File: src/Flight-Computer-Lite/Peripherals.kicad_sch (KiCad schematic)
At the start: 36 parts, among them P3 USB, P4 1984659, Q1 QS5U17TR, Q2 QS5U17TR, U3 SST25VF040B-50-4I-S2AE-T, U4 CP2102-GMR(QFN28), U5 TS391IYLT, U6 BMP390, U7 TS391IYLT, U8 TS391IYLT

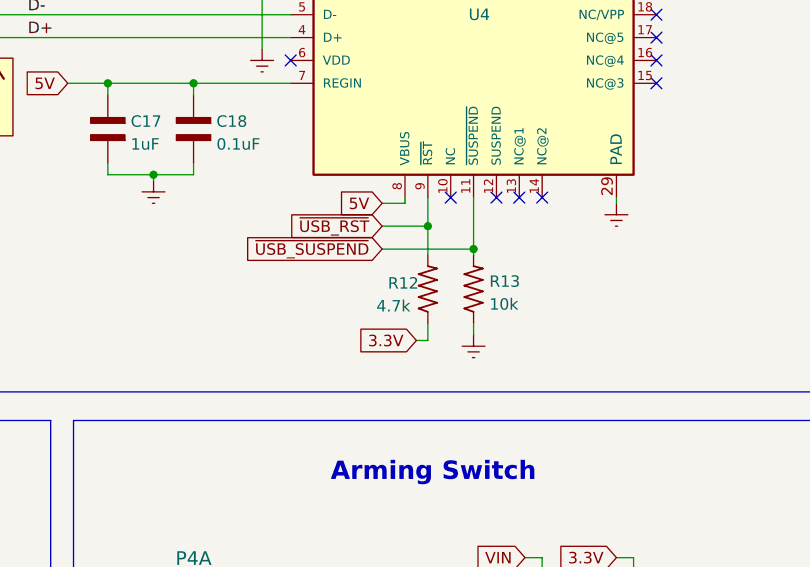
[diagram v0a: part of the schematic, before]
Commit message: imported footprints into layout
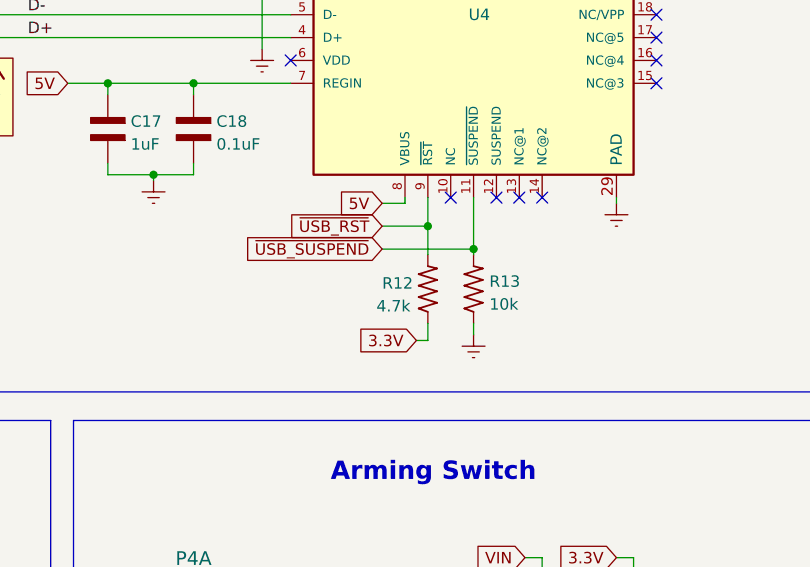
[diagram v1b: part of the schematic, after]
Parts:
- B2: footprint SW_PTS647SM38SMTR2LFS_CNK -> Flight-Computer-Lite:PTS647SM38SMTR2LFS
- BZ1: footprint Flight-Computer:AT-1438-TWT-R -> Flight-Computer-Lite:AT-1438-TWT-R
- C16, C17, C18, C19, C20, C21, C22: footprint Flight-Computer:CAP_0603 -> Flight-Computer-Lite:CAP_0603
- D5: footprint SOD-123FL_MCC -> Flight-Computer-Lite:SP0504BAHTG
- P3: footprint BEL_SS-52300-001 -> Flight-Computer-Lite:10118194-0001LF
- P4: footprint Flight-Computer:1984659 -> Flight-Computer-Lite:1984659
- Q1, Q2: footprint Flight-Computer:QS5U17TR -> Flight-Computer-Lite:QS5U17TR
- R10, R11, R12, R13, R14, R15, R16, R17, R18, R19, R20, R21, R22, R7, R8, R9: footprint Flight-Computer:RES_0603 -> Flight-Computer-Lite:RES_0603
- U3: footprint SOIC8_S2A_SST_MCH -> Flight-Computer-Lite:AT-1438-TWT-R
- U4: footprint QFN28G_0.5-5X5MM -> Flight-Computer-Lite:CP2012-GMR
- U6: footprint XDCR_BMP390L -> Flight-Computer-Lite:CAP_0603

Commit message: finalized board outline and component placements
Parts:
- U3: footprint Flight-Computer-Lite:AT-1438-TWT-R -> Flight-Computer-Lite:SST25VF040B-50-4I-S2AE-T
- U6: footprint Flight-Computer-Lite:CAP_0603 -> Flight-Computer-Lite:BMP390
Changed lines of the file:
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@@
       (effects (font (size 1.524 1.524)) hide)
     )
-    (property "Footprint" "Flight-Computer-Lite:AT-1438-TWT-R" (id 2) (at 49.53 130.81 0)
+    (property "Footprint" "Flight-Computer-Lite:SST25VF040B-50-4I-S2AE-T" (id 2) (at 49.53 130.81 0)
       (effects (font (size 1.524 1.524)) hide)
     )
@@
     (property "Reference" "U6" (id 0) (at 226.06 36.83 0))
     (property "Value" "BMP390" (id 1) (at 226.695 59.69 0))
-    (property "Footprint" "Flight-Computer-Lite:CAP_0603" (id 2) (at 218.44 65.405 0)
+    (property "Footprint" "Flight-Computer-Lite:BMP390" (id 2) (at 218.44 65.405 0)
       (effects (font (size 1.27 1.27)) (justify left bottom) hide)
     )

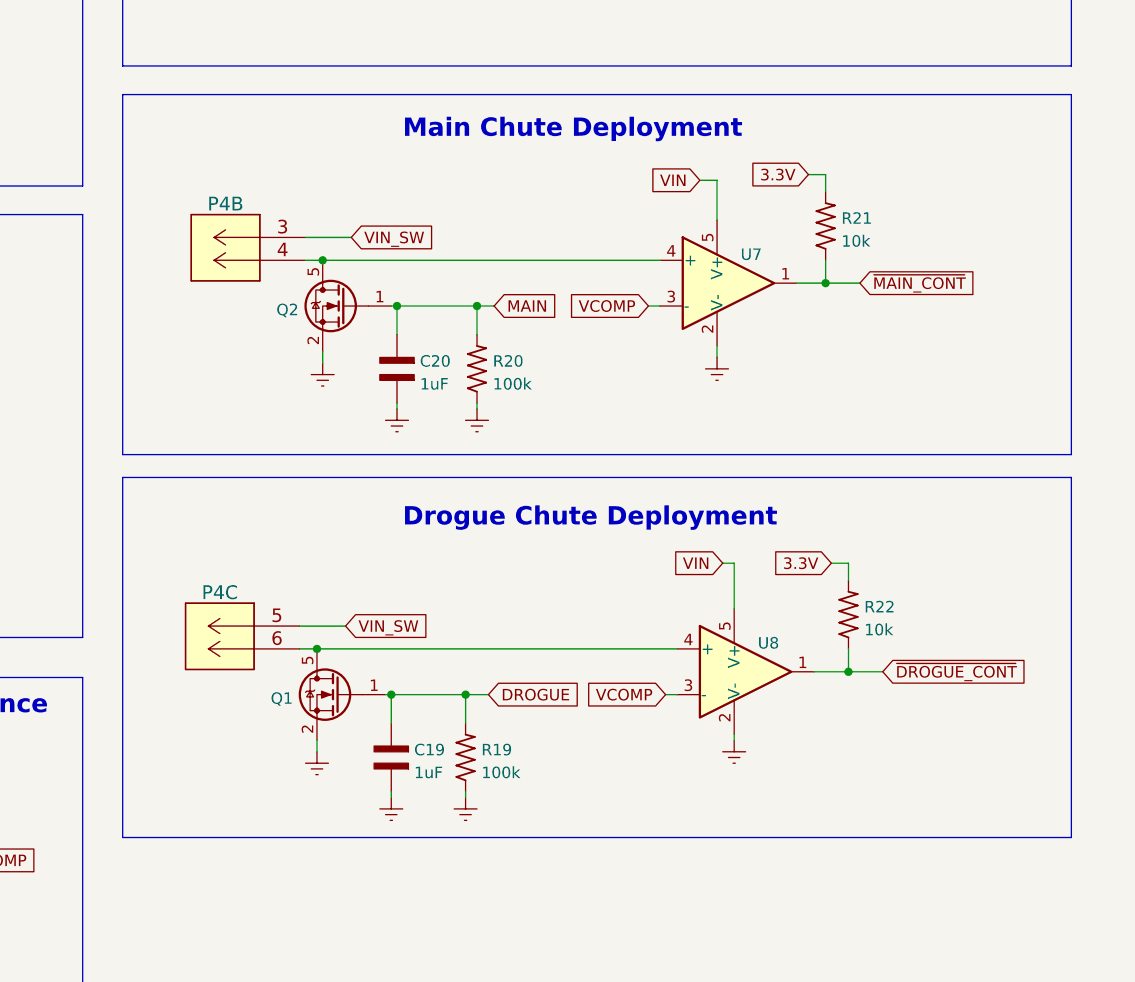
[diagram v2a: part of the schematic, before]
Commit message: added ignition continuity pull down resistors to schematic
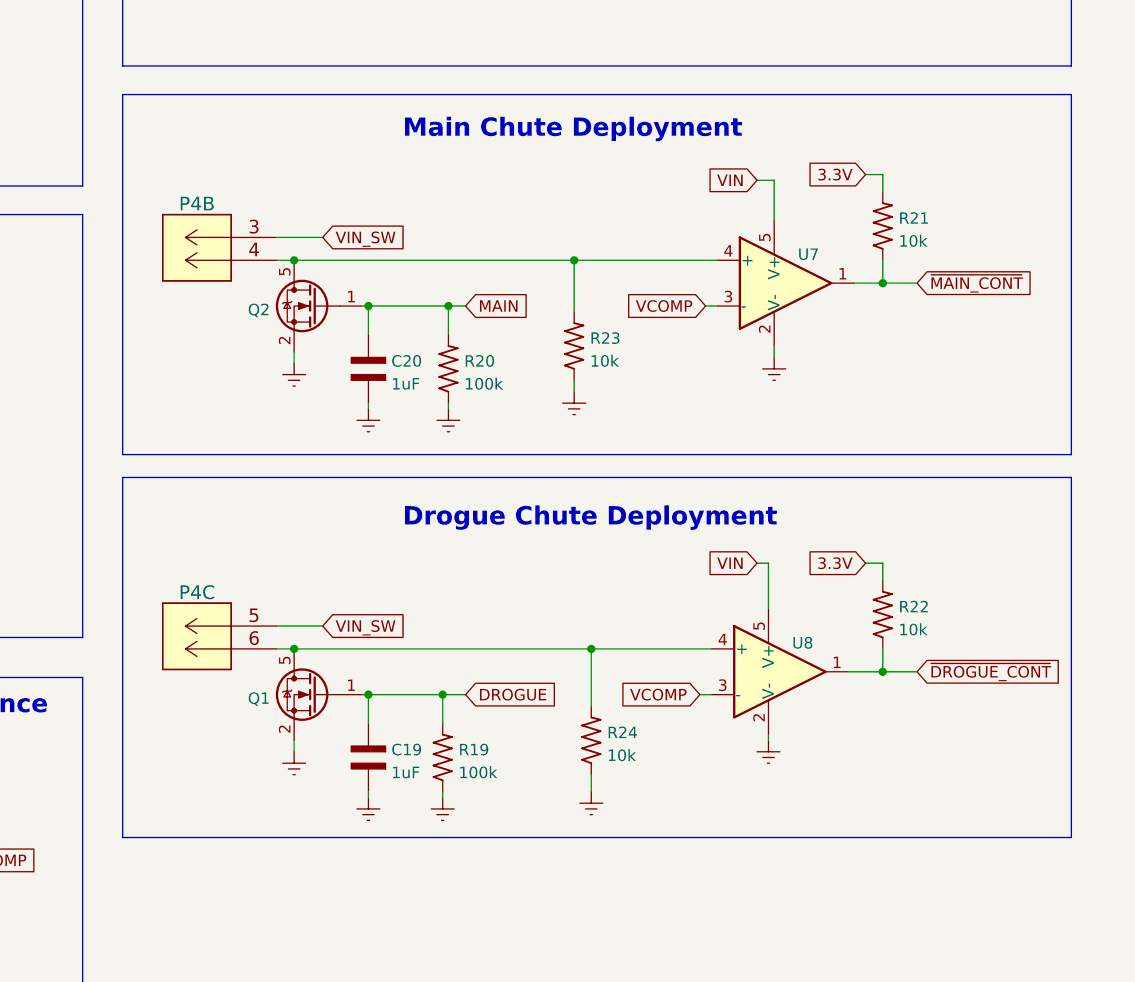
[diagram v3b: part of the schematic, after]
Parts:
- added R23, R24: 10k, Flight-Computer-Lite:RES_0603, symbol Flight-Computer:RES_0603
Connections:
- net Earth: now also R23.1, R24.1
- net at P4.4 (6), Q2.5 (D), U7.4 (+): now also R23.2
- net at P4.6, Q1.5 (D), U8.4 (+): now also R24.2
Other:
- moved on the sheet: C19, C20, P4B, P4C, Q1, Q2, R19, R20, R21, R22, U7, U8
